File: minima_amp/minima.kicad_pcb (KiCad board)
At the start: 2 copper layers, 78 x 60 mm, 40 parts, among them J1 input, J2 output, J3 powersupply, U1 LM1875

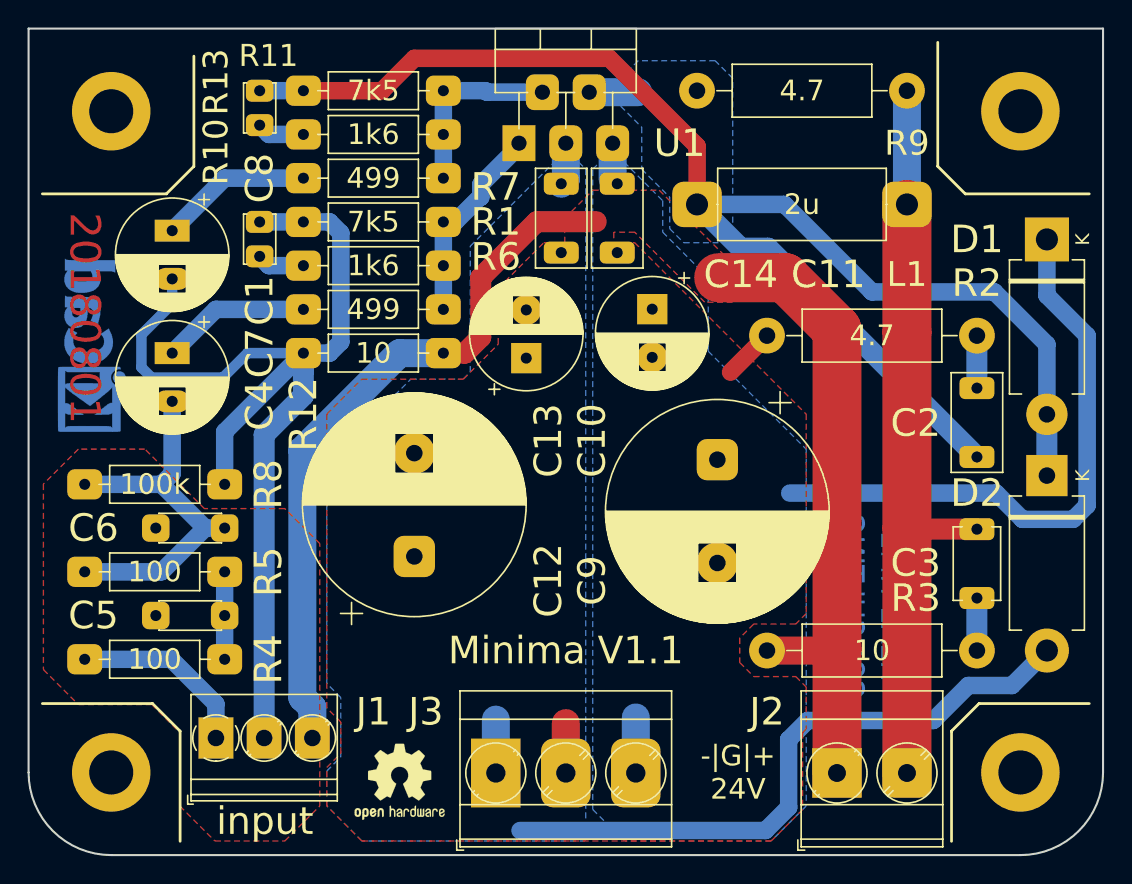
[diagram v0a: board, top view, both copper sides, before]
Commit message: Reworked ground pour aroung SGND input.
Signed-off-by: Nenad Radulovic <nenad.b.radulovic@gmail.com>
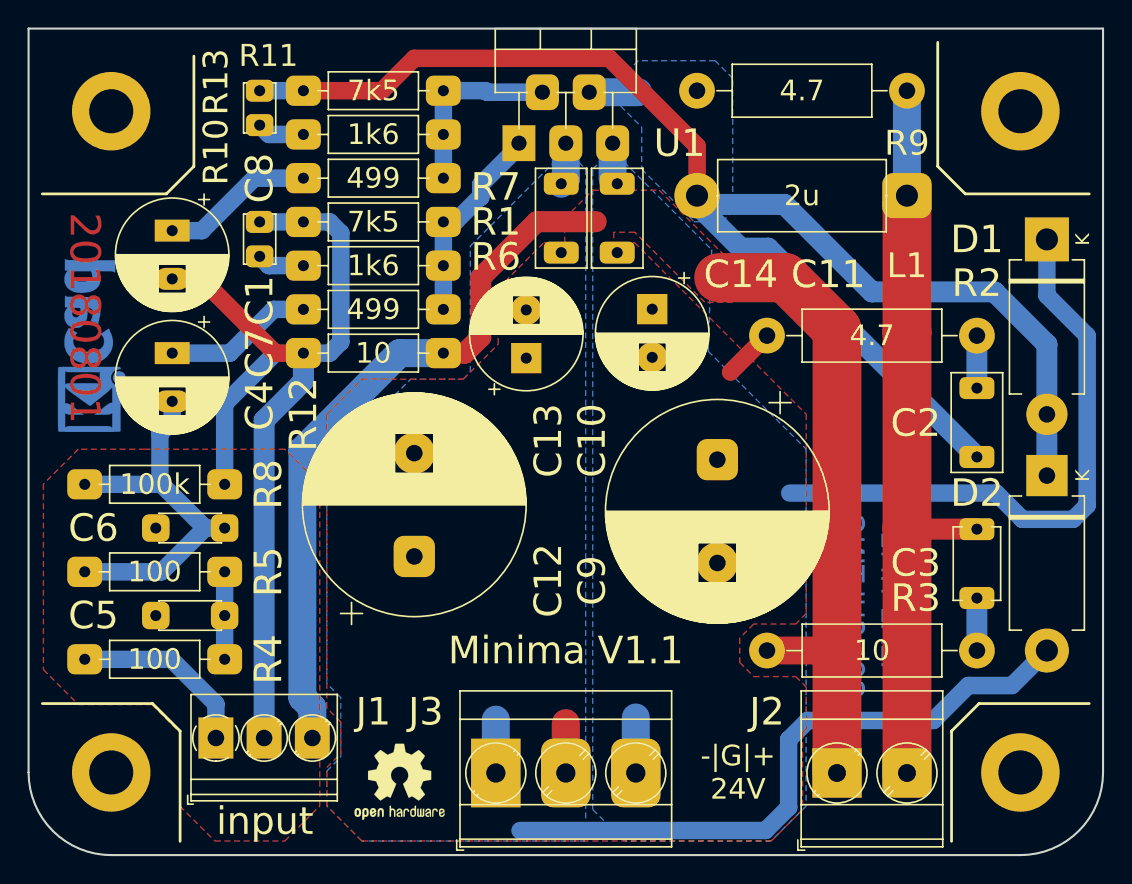
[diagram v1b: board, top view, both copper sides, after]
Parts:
- moved L1 0.63 mm to (155.1, 57.9)
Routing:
- net /sgnd: track 78.4 -> 71.1 mm
